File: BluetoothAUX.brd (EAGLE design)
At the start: 22.2 x 24.4 mm, 19 parts, among them IC2 TPA6132A2, J3 AUDIO_JACK_TRRSSMD_RA, J4 USB, Q1 FDV301N

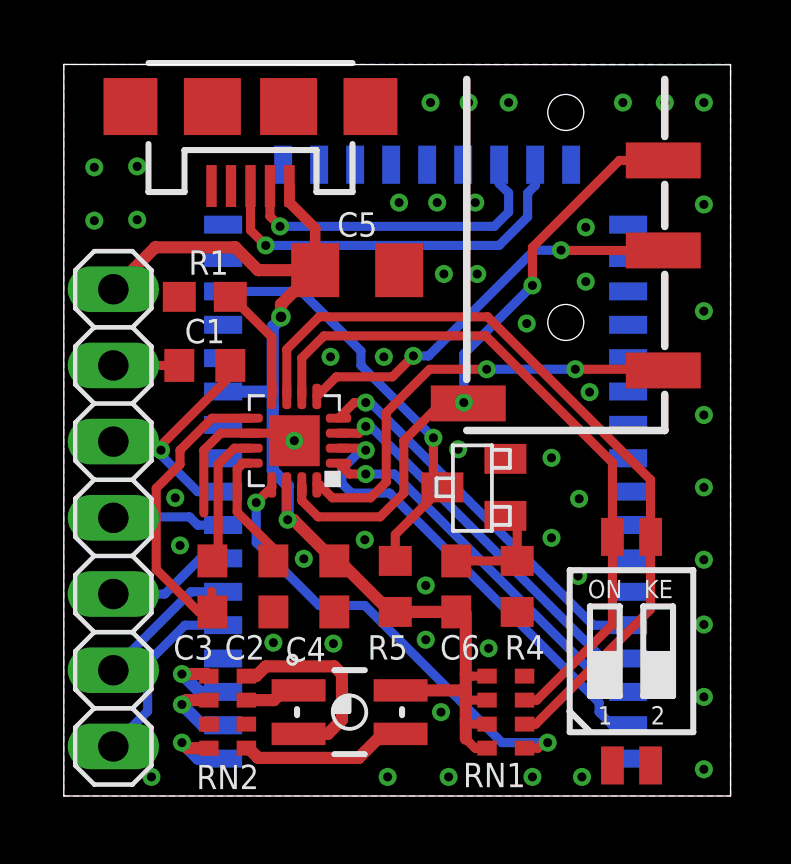
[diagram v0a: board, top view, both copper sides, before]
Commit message: Apply Smart Prototyping DRC
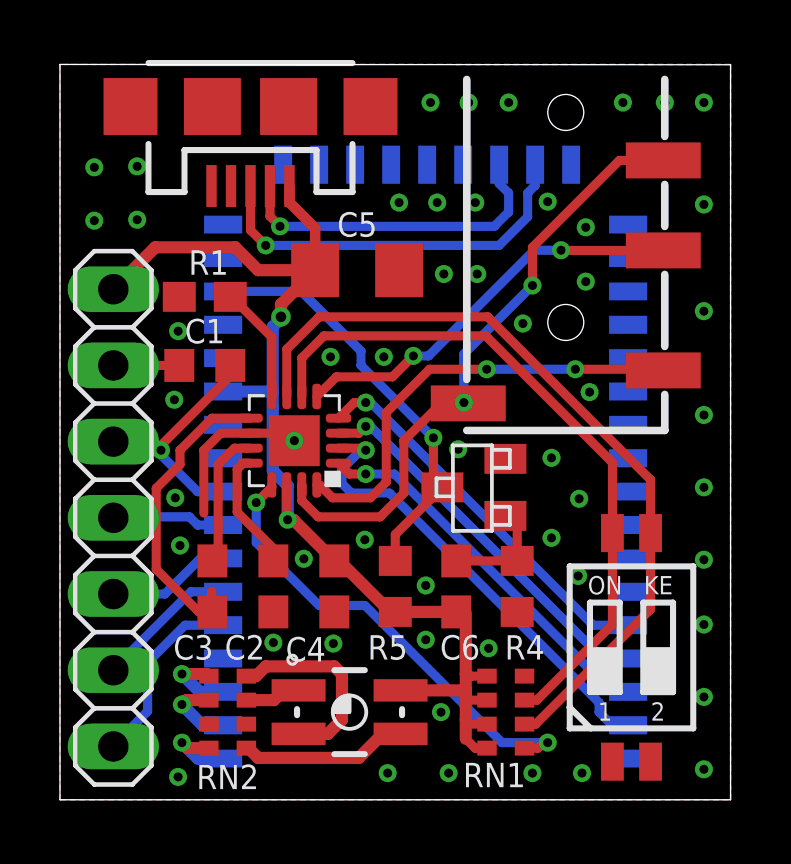
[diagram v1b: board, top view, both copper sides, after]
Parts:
- moved S2 0.13 mm to (90.9, 26.3)
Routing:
- net GND: vias 50 -> 53
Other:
- board size 22.2 x 24.4 mm -> 22.4 x 24.5 mm

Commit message: silk update
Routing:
- net CPN: track 10.2 -> 9.54 mm
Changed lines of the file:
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@@
 </element>
 <element name="C1" library="resistor" library_urn="urn:adsk.eagle:library:348" package="C0603" package3d_urn="urn:adsk.eagle:package:26138/1" value="1uF" x="76.708" y="37.973" smashed="yes" rot="R180">
-<attribute name="NAME" x="76.708" y="36.83" size="0.8128" layer="25" font="vector" rot="R180" align="center"/>
+<attribute name="NAME" x="76.708" y="39.116" size="0.8128" layer="25" font="vector" rot="R180" align="center"/>
 <attribute name="VALUE" x="77.343" y="39.878" size="1.27" layer="27" rot="R180"/>
 </element>
@@
 </element>
 <element name="R1" library="resistor" library_urn="urn:adsk.eagle:library:348" package="R0603" package3d_urn="urn:adsk.eagle:package:26057/1" value="10K" x="76.708" y="35.687" smashed="yes">
-<attribute name="NAME" x="76.835" y="39.116" size="0.8128" layer="25" font="vector" align="center"/>
+<attribute name="NAME" x="77.089" y="36.83" size="0.8128" layer="25" font="vector" align="center"/>
 <attribute name="VALUE" x="76.073" y="33.782" size="1.27" layer="27"/>
 </element>
@@
 <contactref element="J4" pad="P$2"/>
 <via x="93.345" y="44.45" extent="1-16" drill="0.3"/>
-<via x="85.7885" y="38.735" extent="1-16" drill="0.3"/>
+<via x="88.0745" y="38.481" extent="1-16" drill="0.3"/>
 <via x="75.72375" y="31.27375" extent="1-16" drill="0.3"/>
 <via x="73.025" y="40.513" extent="1-16" drill="0.3"/>
@@
 <via x="79.6925" y="33.17875" extent="1-16" drill="0.3"/>
 <via x="86.1695" y="26.25725" extent="1-16" drill="0.3"/>
-<via x="87.3125" y="37.084" extent="1-16" drill="0.3"/>
+<via x="85.6615" y="38.989" extent="1-16" drill="0.3"/>
 <via x="89.408" y="40.29075" extent="1-16" drill="0.3"/>
 <wire x1="78.2175" y1="33.42875" x2="79.4425" y2="33.42875" width="0.3048" layer="1"/>
@@
 <wire x1="82.96275" y1="35.306" x2="83.66125" y2="36.0045" width="0.3048" layer="1"/>
 <wire x1="81.09475" y1="35.306" x2="82.96275" y2="35.306" width="0.3048" layer="1"/>
-<wire x1="88.5825" y1="39.52875" x2="87.6935" y2="39.52875" width="0.3048" layer="16"/>
-<wire x1="87.6935" y1="39.52875" x2="84.16925" y2="36.0045" width="0.3048" layer="16"/>
-<wire x1="84.16925" y1="36.0045" x2="83.66125" y2="36.0045" width="0.3048" layer="16"/>
+<wire x1="88.5825" y1="39.52875" x2="87.1855" y2="39.52875" width="0.3048" layer="16"/>
+<wire x1="87.1855" y1="39.52875" x2="83.66125" y2="36.0045" width="0.3048" layer="16"/>
 </signal>
 <signal name="OUTL">
@@
 <contactref element="IC2" pad="9"/>
 <contactref element="C3" pad="2"/>
-<wire x1="76.962" y1="27.471" x2="76.9375" y2="28.155" width="0.3048" layer="1"/>
 <wire x1="78.2175" y1="33.92875" x2="76.95" y2="33.92875" width="0.3048" layer="1"/>
 <wire x1="76.95" y1="33.92875" x2="75.8825" y2="32.86125" width="0.3048" layer="1"/>
@@
 <wire x1="86.0975" y1="34.44875" x2="85.49125" y2="34.42" width="0.3048" layer="1"/>
 <wire x1="91.99125" y1="42.52" x2="90.526" y2="42.52" width="0.3048" layer="1"/>
-<wire x1="90.526" y1="42.52" x2="87.63" y2="39.624" width="0.3048" layer="1"/>
-<wire x1="87.63" y1="39.624" x2="87.63" y2="38.354" width="0.3048" layer="1"/>
-<via x="87.63" y="38.354" extent="1-16" drill="0.3"/>
-<wire x1="87.63" y1="38.354" x2="85.344" y2="36.068" width="0.3048" layer="16"/>
+<wire x1="90.526" y1="42.52" x2="87.122" y2="39.116" width="0.3048" layer="1"/>
+<wire x1="87.122" y1="39.116" x2="87.122" y2="37.338" width="0.3048" layer="1"/>
+<via x="87.122" y="37.338" extent="1-16" drill="0.3"/>
 <via x="85.344" y="34.44875" extent="1-16" drill="0.3"/>
-<wire x1="85.344" y1="36.068" x2="85.344" y2="34.44875" width="0.3048" layer="16"/>
+<wire x1="86.868" y1="37.338" x2="87.122" y2="37.338" width="0.3048" layer="16"/>
+<wire x1="85.344" y1="34.44875" x2="85.344" y2="35.814" width="0.3048" layer="16"/>
+<wire x1="85.344" y1="35.814" x2="86.868" y2="37.338" width="0.3048" layer="16"/>
 </signal>
 <signal name="N$2">
